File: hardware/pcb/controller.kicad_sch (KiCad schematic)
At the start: 17 parts, among them J1 USB_C_Receptacle_USB2.0_16P, J2 Micro_SD_Card, SW1 SW_Push, SW2 SW_Push, SW3 SW_SPDT, U1 ESP32-WROOM-32, U2 SX1262IMLTRT, U3 BQ25185DLHR, U4 PE4259, U5 AP2112K-3.3, U6 NHD-C12832A1Z-FSRGB, Y1 32.768KHz, Y2 32MHz

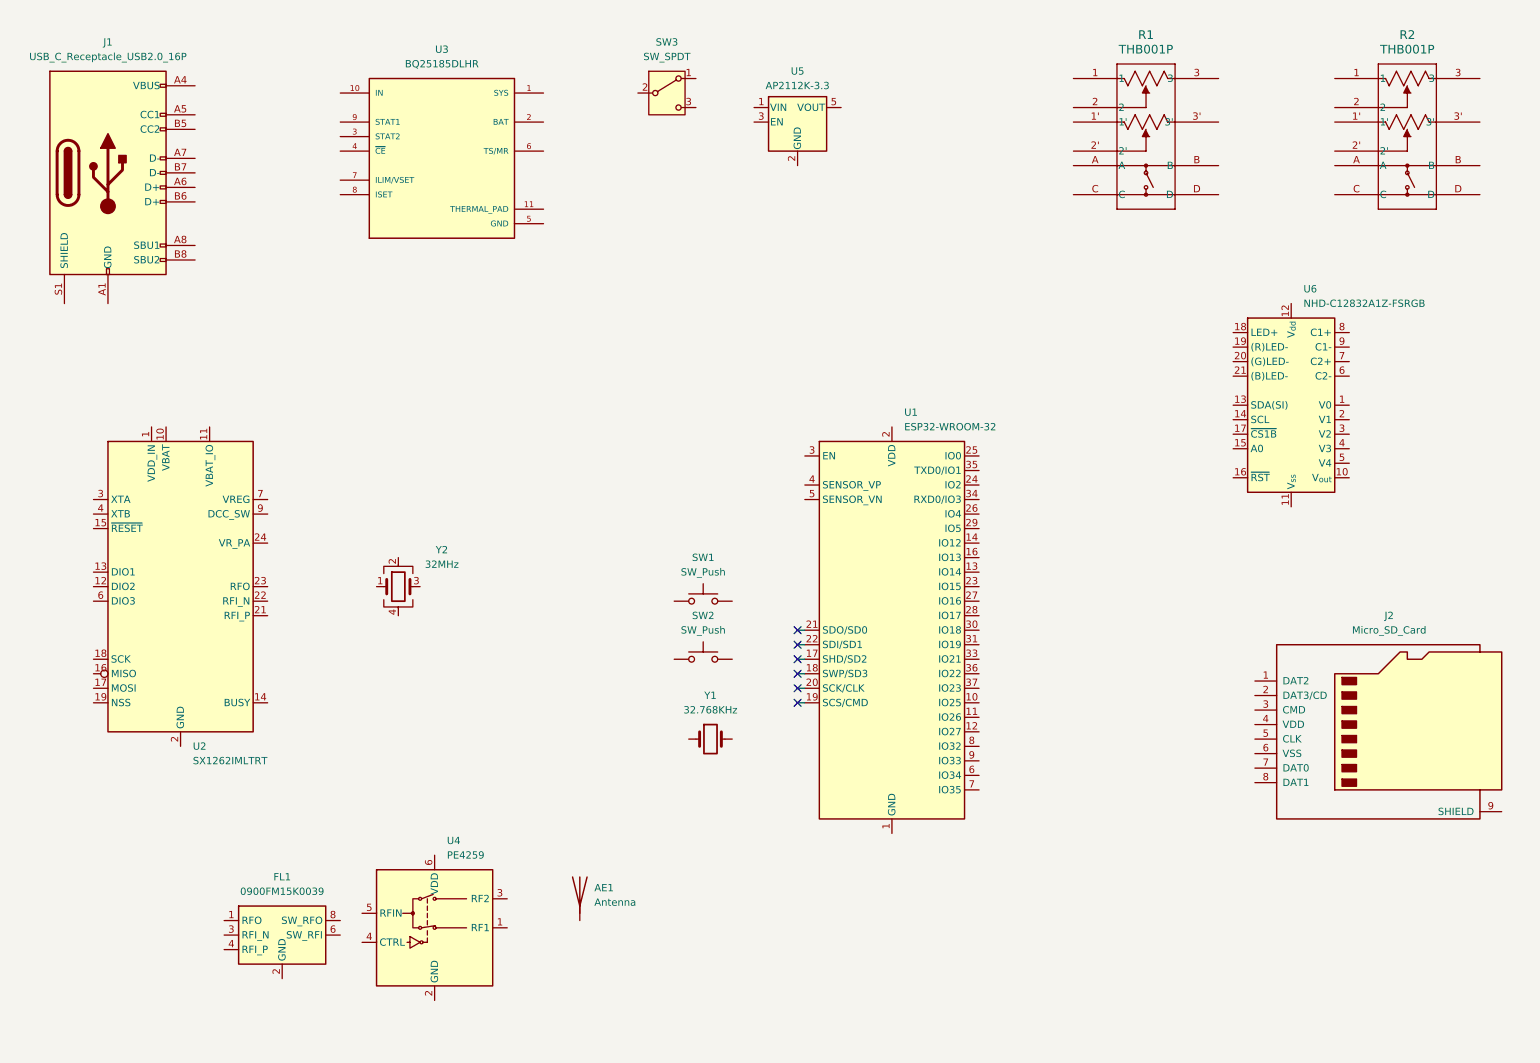
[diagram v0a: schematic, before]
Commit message: started wiring schematic
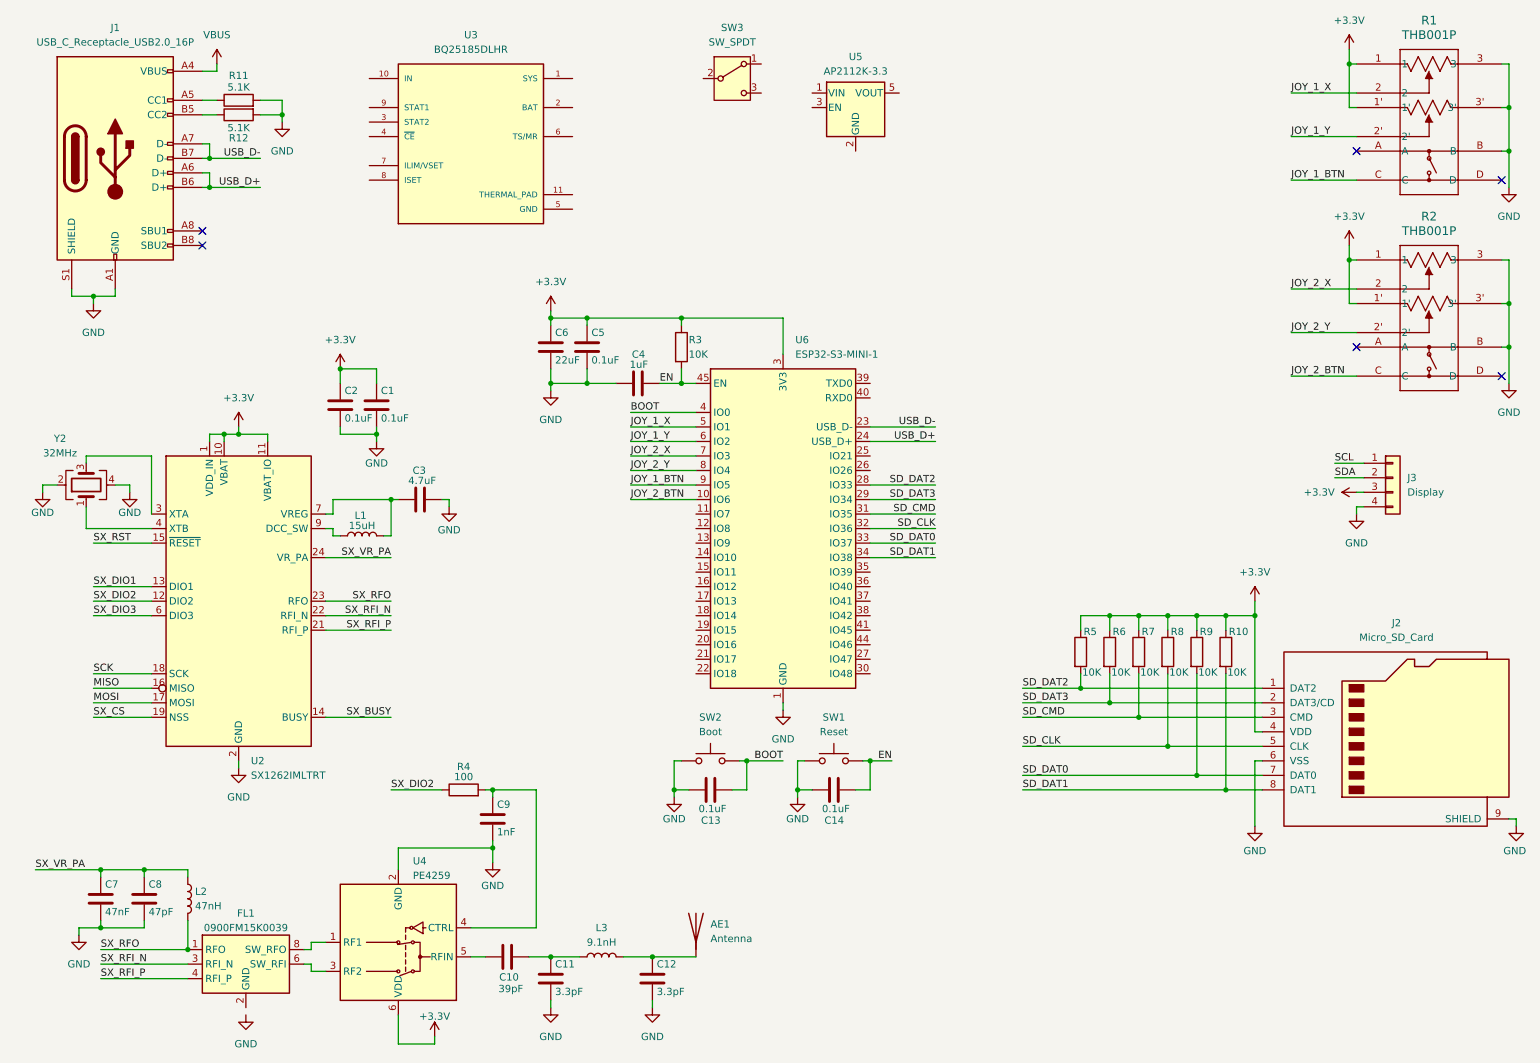
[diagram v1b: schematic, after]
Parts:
- removed U1: ESP32-WROOM-32, RF_Module:ESP32-WROOM-32, symbol RF_Module:ESP32-WROOM-32
- removed U6: NHD-C12832A1Z-FSRGB, Display:NHD-C12832A1Z-FSRGB, symbol Display_Graphic:NHD-C12832A1Z-FSRGB
- removed Y1: 32.768KHz, symbol Device:Crystal
- added C1, C13, C14, C2, C5: 0.1uF, symbol Device:C
- added C10: 39pF, symbol Device:C
- added C11, C12: 3.3pF, symbol Device:C
- added C3: 4.7uF, symbol Device:C
- added C4: 1uF, symbol Device:C
- added C6: 22uF, symbol Device:C
- added C7: 47nF, symbol Device:C
- added C8: 47pF, symbol Device:C
- added C9: 1nF, symbol Device:C
- added J3: Display, symbol Connector_Generic:Conn_01x04
- added L1: 15uH, symbol Device:L
- added L2: 47nH, symbol Device:L
- added L3: 9.1nH, symbol Device:L
- added R10, R3, R5, R6, R7, R8, R9: 10K, symbol Device:R
- added R11, R12: 5.1K, symbol Device:R
- added R4: 100, symbol Device:R
- added U6: ESP32-S3-MINI-1, RF_Module:ESP32-S2-MINI-1, symbol RF_Module:ESP32-S3-MINI-1
- SW1: value SW_Push -> Reset
- SW2: value SW_Push -> Boot
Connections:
- net +3.3V: now reaches R2.1
- net +3.3V: now also J2.4 (VDD), R1.1, R1.1', R2.1', U2.1 (VDD_IN), U2.10 (VBAT), U2.11 (VBAT_IO), U4.6 (VDD), C1.1, C2.1, C5.1, C6.1, J3.3 (Pin_3), R10.1, R3.1, R5.1, R6.1, R7.1, R8.1, R9.1, U6.3 (3V3)
- net JOY_2_X: now reaches R2.2
- net JOY_2_X: now also U6.7 (IO3)
- net JOY_2_Y: now reaches R2.2'
- net JOY_2_Y: now also U6.8 (IO4)
- net GND: now reaches R2.3
- net GND: now also J1.A1 (GND), J1.A12 (GND), J1.B1 (GND), J1.B12 (GND), J1.S1 (SHIELD), J2.6 (VSS), J2.9 (SHIELD), R1.3, R1.3', R1.B, R2.3', R2.B, SW1.1, SW2.1, U2.2 (GND), U2.20 (GND), U2.25 (GND), U2.5 (GND), U2.8 (GND), U4.2 (GND), Y2.2, Y2.4, C1.2, C11.2, C12.2, C13.1, C14.1, C2.2, C3.2, C4.1, C5.2, C6.2, C7.2, C8.2, C9.2, J3.4 (Pin_4), R11.2, R12.2, U6.1 (GND), U6.2 (GND), U6.42 (GND), U6.43 (GND), U6.46 (GND), U6.47 (GND), U6.48 (GND), U6.49 (GND), U6.50 (GND), U6.51 (GND), U6.52 (GND), U6.53 (GND), U6.54 (GND), U6.55 (GND), U6.56 (GND), U6.57 (GND), U6.58 (GND), U6.59 (GND), U6.60 (GND), U6.61 (GND), U6.62 (GND), U6.63 (GND), U6.64 (GND), U6.65 (GND)
- net JOY_2_BTN: now reaches R2.C
- net JOY_2_BTN: now also U6.10 (IO6)
- net SD_DAT2: now reaches J2.1 (DAT2)
- net SD_DAT2: now also R5.2, U6.28 (IO33)
- net SD_DAT3: now reaches J2.2 (DAT3/CD)
- net SD_DAT3: now also R6.2, U6.29 (IO34)
- net SD_CMD: now reaches J2.3 (CMD)
- net SD_CMD: now also R7.2, U6.31 (IO35)
- net SD_CLK: now reaches J2.5 (CLK)
- net SD_CLK: now also R8.2, U6.32 (IO36)
- net SD_DAT0: now reaches J2.7 (DAT0)
- net SD_DAT0: now also R9.2, U6.33 (IO37)
- net SD_DAT1: now reaches J2.8 (DAT1)
- net SD_DAT1: now also R10.2, U6.34 (IO38)
- net BOOT: now reaches SW2.2
- net BOOT: now also C13.2, U6.4 (IO0)
- net at U4.1 (RF1): now also FL1.8 (SW_RFO)
- net at U4.3 (RF2): now also FL1.6 (SW_RFI)
- net at U4.4 (CTRL): now also C9.1, R4.2
- net at U4.5 (RFIN): now also C10.1
- net VBUS: now reaches J1.A4 (VBUS), J1.A9 (VBUS), J1.B4 (VBUS), J1.B9 (VBUS)
- net at J1.A5 (CC1): now also R11.1
- net USB_D+: now reaches J1.A6 (D+)
- net USB_D+: now also J1.B6 (D+), U6.24 (USB_D+)
- net USB_D-: now reaches J1.A7 (D-)
- net USB_D-: now also J1.B7 (D-), U6.23 (USB_D-)
- net at J1.B5 (CC2): now also R12.1
- net JOY_1_X: now reaches R1.2
- net JOY_1_X: now also U6.5 (IO1)
- net JOY_1_Y: now reaches R1.2'
- net JOY_1_Y: now also U6.6 (IO2)
- net JOY_1_BTN: now reaches R1.C
- net JOY_1_BTN: now also U6.9 (IO5)
- net EN: now reaches SW1.2
- net EN: now also C14.2, C4.2, R3.2, U6.45 (EN)
- net at AE1.1 (A): now also C12.1, L3.2
- net at Y2.1: now also U2.4 (XTB)
- net at Y2.3: now also U2.3 (XTA)
- net SX_DIO2: now reaches U2.12 (DIO2)
- net SX_DIO2: now also R4.1
- net SX_DIO1: now reaches U2.13 (DIO1)
- net SX_BUSY: now reaches U2.14 (BUSY)
- net SX_RST: now reaches U2.15 (~{RESET})
- net MISO: now reaches U2.16 (MISO)
- net MOSI: now reaches U2.17 (MOSI)
- net SCK: now reaches U2.18 (SCK)
- net SX_CS: now reaches U2.19 (NSS)
- net SX_RFI_P: now reaches U2.21 (RFI_P)
- net SX_RFI_P: now also FL1.4 (RFI_P)
- net SX_RFI_N: now reaches U2.22 (RFI_N)
- net SX_RFI_N: now also FL1.3 (RFI_N)
- net SX_RFO: now reaches U2.23 (RFO)
- net SX_RFO: now also FL1.1 (RFO), L2.2
- net SX_VR_PA: now reaches U2.24 (VR_PA)
- net SX_VR_PA: now also C7.1, C8.1, L2.1
- net SX_DIO3: now reaches U2.6 (DIO3)
- net at U2.7 (VREG): now also C3.1, L1.2
- net at U2.9 (DCC_SW): now also L1.1
- new net: C10.2, C11.1, L3.1
- new net SCL: J3.1 (Pin_1)
- new net SDA: J3.2 (Pin_2)
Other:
- moved on the sheet: AE1, FL1, J1, R1, SW1, SW2, SW3, U2, U3, U4, U5, Y2

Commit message: finished schematic
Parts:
- removed U3: BQ25185DLHR, BQ25185DLHR:IC_BQ25185DLHR, symbol Imports:BQ25185DLHR
- removed U5: AP2112K-3.3, Package_TO_SOT_SMD:SOT-23-5, symbol Regulator_Linear:AP2112K-3.3
- added BT1, BT2: Battery_Cell, symbol Device:Battery_Cell
- added C15: 2.2uF, symbol Device:C
- added C16, C17: 0.1uF, symbol Device:C
- added C18: 10uF, symbol Device:C
- added C19, C20, C23: 22uF, symbol Device:C
- added C21, C22: 1uF, symbol Device:C
- added C24, C25: 33uF, symbol Device:C
- added D1, D2: LED, symbol Device:LED
- added L4: 1.5uH, symbol Device:L
- added L5: 10uH, symbol Device:L
- added R13, R21: 10K, symbol Device:R
- added R14: 28.7K, symbol Device:R
- added R15, R16, R20: 2K, symbol Device:R
- added R17: 12K, symbol Device:R
- added R18: 12.62K, symbol Device:R
- added R19: 3K, symbol Device:R
- added R22: 5.5K, symbol Device:R
- added R23: 31.6K, symbol Device:R
- added R24: 10.2, symbol Device:R
- added SW4: EStop, symbol Switch:SW_Push
- added TH1: NTCG, Resistor_SMD:R_0402_1005Metric, symbol Device:Thermistor
- added U3: MP2672AGD-0000-Z, QFN-18_MP2672A_MNP, symbol Imports:MP2672AGD-0000-Z
- added U5: LMR51625XDDCR, DDC0006A-MFG, symbol Imports:LMR51625XDDCR
- R1, R2: footprint Imports:THB001P_CNK -> THB001P_CNK
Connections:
- net +3.3V: now also C24.1, C25.1, L5.2, R15.1, R16.2, U3.17 (CV)
- net GND: now also BT2.2 (-), C15.2, C18.2, C19.2, C20.2, C21.2, C23.2, C24.2, C25.2, R14.2, R17.2, R22.2, R24.2, SW4.1, TH1.2, U3.13 (PGND), U5.4 (GND)
- net SCL: now also U6.13 (IO9), U3.15 (SDA)
- net SDA: now also U6.12 (IO8), U3.14 (SCL)
- net VBUS: now also C18.1, L4.1, R13.1, U3.1 (IN)
- net BAT_ADC: now reaches U6.11 (IO7)
- net BAT_ADC: now also R21.2, R22.1
- net ESTOP: now reaches U6.22 (IO18)
- net ESTOP: now also SW4.2
- net VCC: now reaches SW3.2 (B)
- net VCC: now also C19.1, C20.1, C21.1, U3.11 (SYS)
- net at SW3.3 (C): now also C15.1, U5.2 (EN), U5.3 (VIN)
- new net: D2.2 (A), R16.1
- new net: R13.2, R14.1, U3.7 (VLIM)
- new net: R19.2, TH1.1
- new net: D1.1 (K), U3.18 (*ACOK)
- new net: D1.2 (A), R15.2
- new net: BT1.1 (+), C23.1, R21.1, U3.10 (BATT)
- new net: C22.1, R18.1, U3.4 (VCC)
- new net: R18.2, R19.1, U3.8 (NTC)
- new net: D2.1 (K), U3.16 (*STAT)
- new net: C22.2, U3.6 (AGND)
- new net: R23.2, R24.1, U5.1 (FB)
- new net: C16.2, L5.1, U5.5 (SW)
- new net: C16.1, U5.6 (CB)
- new net: C17.1, L4.2, U3.12 (SW), U3.2 (SW)
- new net: C17.2, U3.3 (BST)
- new net: R17.1, U3.5 (ISET)
- new net: R20.1, U3.9 (MID)
- new net: BT1.2 (-), BT2.1 (+), R20.2
- no-connect marks 6 -> 24
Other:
- note added: "Battery Charger"
- note added: "Buck Regulator"
- note added: "Configured for: 1A charge 4.675V min input volage"
- note added: "Couldn't figure out the exact calculation for the thermistor voltage divider but this should be acceptable"
- note added: "ESP32-S3 Module"
- note added: "EStop Button"
- note added: "Joysticks"
- note added: "MicroSD Card"
- note added: "OLED Display"
- note added: "SX1262 LoRa Module"
- note added: "USB Connector"
- moved on the sheet: AE1, C1, C10, C11, C12, C13, C14, C2, C3, C4, C5, C6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

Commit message: added footprints
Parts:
- AE1: footprint (none) -> Connector_Coaxial:SMA_Amphenol_901-143_Horizontal
- BT1, BT2: footprint (none) -> Battery:BatteryHolder_MPD_BH-18650-PC
- C1, C10, C11, C12, C13, C14, C15, C16, C2, C4, C5, C7, C8, C9: footprint (none) -> Capacitor_SMD:C_0402_1005Metric
- C17, C21, C22, C24, C6: footprint (none) -> Capacitor_SMD:C_0603_1608Metric
- C18, C19, C20, C25: footprint (none) -> Capacitor_SMD:C_0805_2012Metric
- C23: footprint (none) -> Capacitor_SMD:C_1206_3216Metric
- C3: value 4.7uF -> 470nF; footprint (none) -> Capacitor_SMD:C_0402_1005Metric
- D1, D2: footprint (none) -> LED_THT:LED_D3.0mm
- J1: footprint (none) -> Connector_USB:USB_C_Receptacle_GCT_USB4105-xx-A_16P_TopMnt_Horizontal
- J2: footprint (none) -> Connector_Card:microSD_HC_Wuerth_693072010801
- J3: footprint (none) -> Connector_JST:JST_PH_S4B-PH-K_1x04_P2.00mm_Horizontal
- L1, L2, L3: footprint (none) -> Inductor_SMD:L_0402_1005Metric
- L4, L5: footprint (none) -> Inductor_SMD:L_6.3x6.3_H3
- R1, R2: footprint THB001P_CNK -> Imports:THB001P_CNK
- R10, R11, R12, R13, R14, R15, R16, R17, R18, R19, R20, R21, R22, R23, R24, R3, R4, R5, R6, R7, R8, R9: footprint (none) -> Resistor_SMD:R_0402_1005Metric
- SW1, SW2, SW4: footprint (none) -> Button_Switch_SMD:SW_Push_SPST_NO_Alps_SKRK
- SW3: footprint (none) -> Button_Switch_THT:SW_Slide_SPDT_Straight_CK_OS102011MS2Q
- U3: footprint QFN-18_MP2672A_MNP -> Imports:QFN-18_MP2672A_MNP
- U5: footprint DDC0006A-MFG -> Package_TO_SOT_SMD:SOT-23-6
- Y2: footprint (none) -> Crystal:Crystal_SMD_3225-4Pin_3.2x2.5mm

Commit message: added footprints and started layout
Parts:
- removed J2: Micro_SD_Card, Connector_Card:microSD_HC_Wuerth_693072010801, symbol Connector:Micro_SD_Card
- added C26: 0.1uF, Capacitor_SMD:C_0402_1005Metric, symbol Device:C
- added J2: Micro_SD_Card_Det_Hirose_DM3AT, Connector_Card:microSD_HC_Hirose_DM3AT-SF-PEJM5, symbol Connector:Micro_SD_Card_Det_Hirose_DM3AT
- added R25, R26: 27K, Resistor_SMD:R_0402_1005Metric, symbol Device:R
- C17, C21, C22: footprint Capacitor_SMD:C_0603_1608Metric -> Capacitor_SMD:C_0402_1005Metric
- C18, C19, C20, C25: footprint Capacitor_SMD:C_0805_2012Metric -> Capacitor_SMD:C_0603_1608Metric
- C23: footprint Capacitor_SMD:C_1206_3216Metric -> Capacitor_SMD:C_0805_2012Metric
- L5: footprint Inductor_SMD:L_6.3x6.3_H3 -> Inductor_SMD:L_APV_ANR4010
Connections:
- net +3.3V: now also R23.1, J2.4 (VDD)
- net ESTOP: now also C26.2
- net GND: now also C22.2, FL1.10 (GND), FL1.2 (GND), FL1.5 (GND), FL1.7 (GND), FL1.9 (GND), U3.6 (AGND), C26.1, J2.11 (SHIELD), J2.6 (VSS)
- net SD_CLK: now also J2.5 (CLK)
- net SD_CMD: now also J2.3 (CMD)
- net SD_DAT0: now also U6.35 (IO39), J2.7 (DAT0)
- net SD_DAT1: now also U6.36 (IO40), J2.8 (DAT1)
- net SD_DAT2: now also J2.1 (DAT2)
- net SD_DAT3: now also J2.2 (DAT3/CD)
- net USB_D+: now also R26.1; no longer U6.24 (USB_D+)
- net USB_D-: now also R25.2; no longer U6.23 (USB_D-)
- new net: R26.2, U6.24 (USB_D+)
- new net: R25.1, U6.23 (USB_D-)
- new net SD_DET_1: J2.10 (DET_A), J2.9 (DET_B)
- no-connect marks 24 -> 22
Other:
- moved on the sheet: SW4
